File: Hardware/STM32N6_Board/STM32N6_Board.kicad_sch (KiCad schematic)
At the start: 0 parts

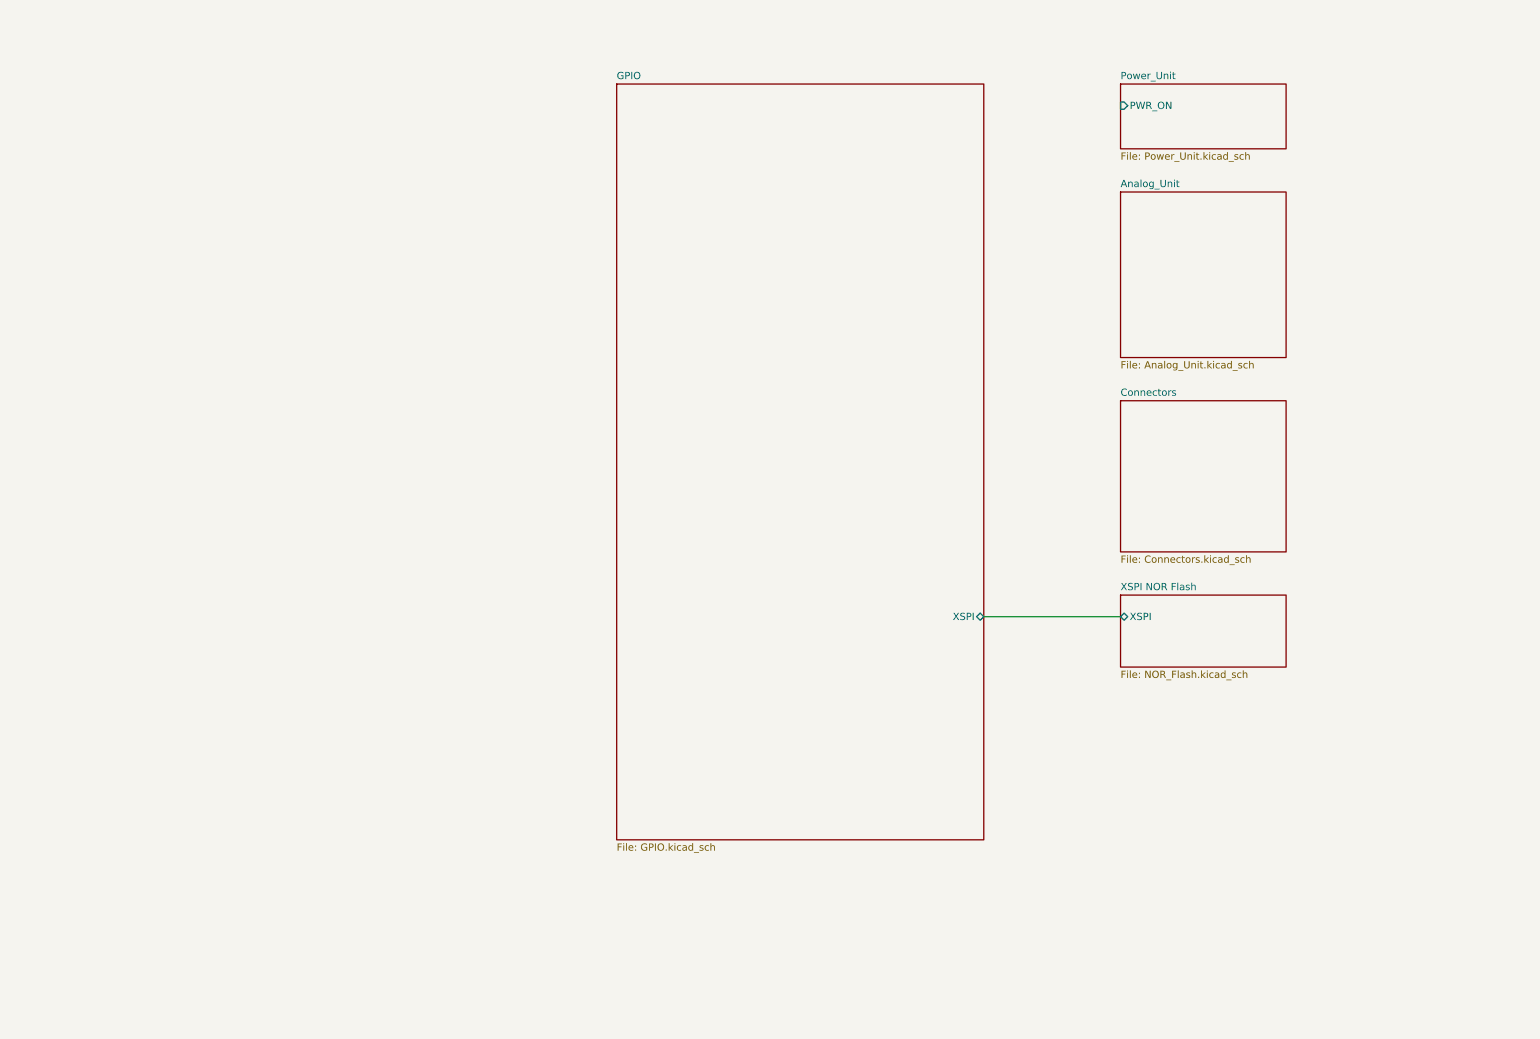
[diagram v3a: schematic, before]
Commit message: Completed wiring of the Analog unit.
- CSI and USB buses are created, yet to be connected with connectors
- Next will be pin selection, and drawing in FMC SDRAM
- Then will be routing GPIOs as buses, and connecting with connectors
- Finally, board layout.
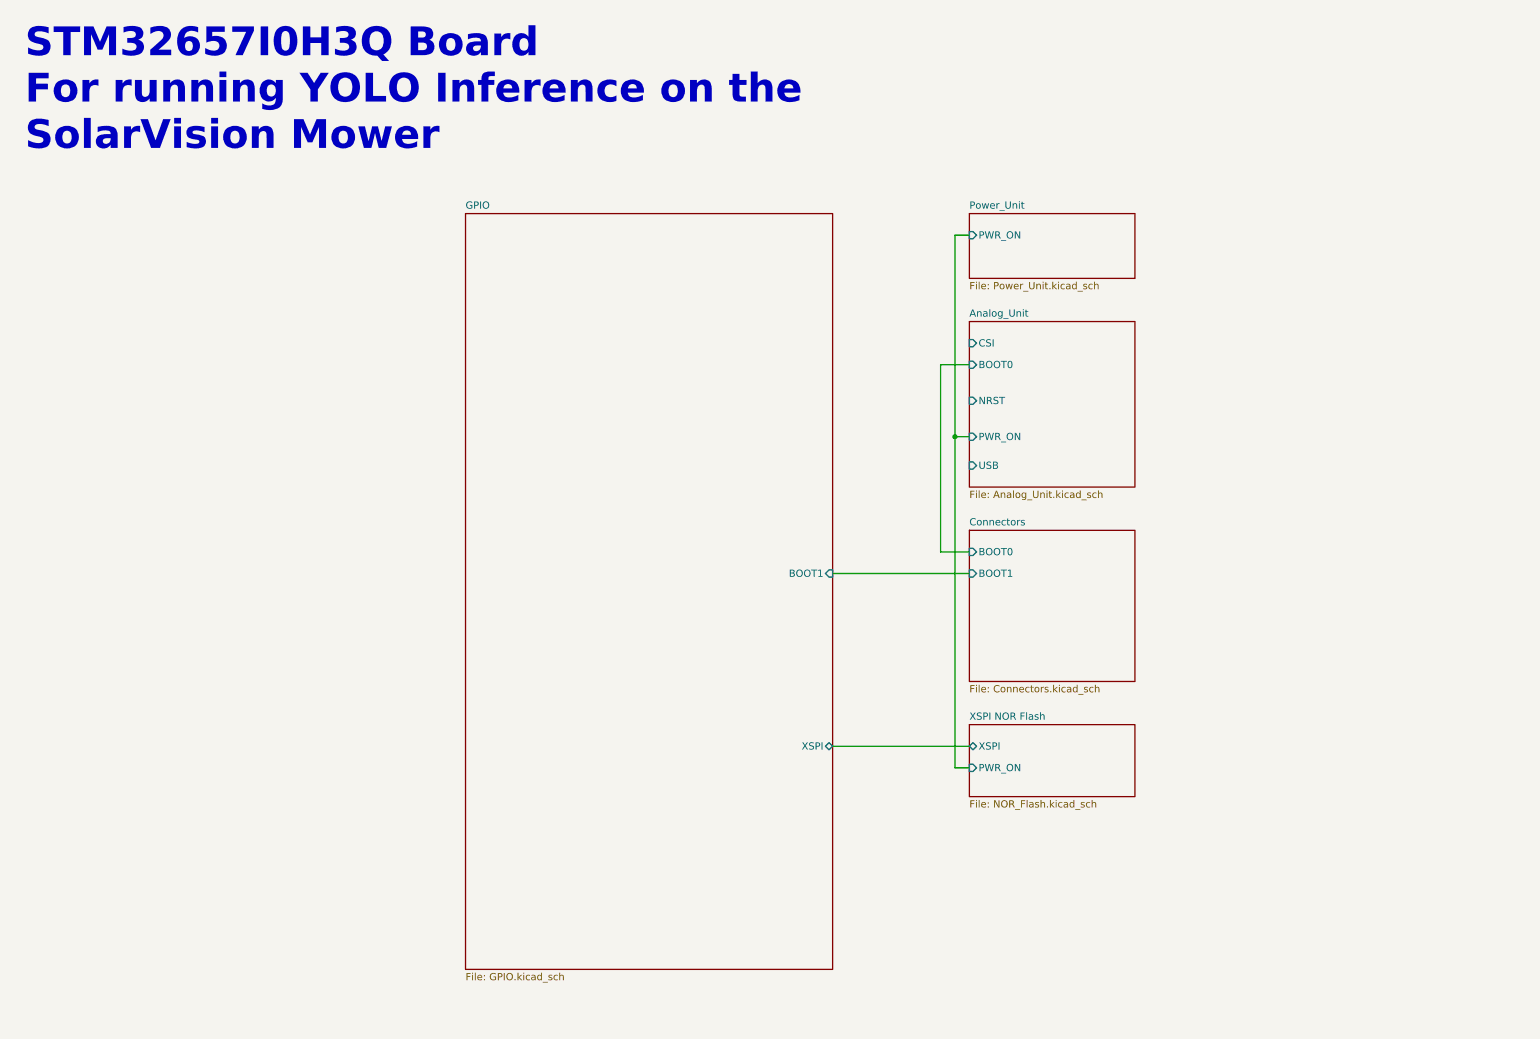
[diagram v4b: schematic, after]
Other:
- sheet Analog_Unit ports: added BOOT0, CSI, NRST, PWR_ON, USB; removed none
- sheet Connectors ports: added BOOT0, BOOT1; removed none
- sheet GPIO ports: added BOOT1; removed none
- sheet XSPI NOR Flash ports: added PWR_ON; removed none
- note added: "STM32657I0H3Q Board For running YOLO Inference on the SolarVision Mower"
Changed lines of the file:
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@@
 		(comment 1 "https://github.com/SolarVisionMower/SolarVision")
 	)
-	(wire
-		(pts
-			(xy 187.96 123.19) (xy 212.09 123.19)
+	(text "STM32657I0H3Q Board\nFor running YOLO Inference on the\nSolarVision Mower"
+		(exclude_from_sim no)
+		(at 18.796 19.05 0)
+		(effects
+			(font
+				(size 5.08 5.08)
+				(thickness 1.016)
+				(bold yes)
+			)
+			(justify left top)
+		)
+	)
+	(junction
+		(at 182.88 91.44)
+		(diameter 0)
+		(color 0 0 0 0)
+	)
+	(wire
+		(pts
+			(xy 182.88 55.88) (xy 182.88 91.44)
+		)
+		(stroke
+			(width 0)
+			(type default)
+		)
+	)
+	(wire
+		(pts
+			(xy 161.29 115.57) (xy 185.42 115.57)
+		)
+		(stroke
+			(width 0)
+			(type default)
+		)
+	)
+	(wire
+		(pts
+			(xy 182.88 149.86) (xy 182.88 91.44)
+		)
+		(stroke
+			(width 0)
+			(type default)
+		)
+	)
+	(wire
+		(pts
+			(xy 180.34 78.74) (xy 180.34 111.76)
+		)
+		(stroke
+			(width 0)
+			(type default)
+		)
+	)
+	(wire
+		(pts
+			(xy 161.29 146.05) (xy 185.42 146.05)
+		)
+		(stroke
+			(width 0)
+			(type default)
+		)
+	)
+	(wire
+		(pts
+			(xy 185.42 149.86) (xy 182.88 149.86)
+		)
+		(stroke
+			(width 0)
+			(type default)
+		)
+	)
+	(wire
+		(pts
+			(xy 185.42 55.88) (xy 182.88 55.88)
+		)
+		(stroke
+			(width 0)
+			(type default)
+		)
+	)
+	(wire
+		(pts
+			(xy 185.42 78.74) (xy 180.34 78.74)
+		)
+		(stroke
+			(width 0)
+			(type default)
+		)
+	)
+	(wire
+		(pts
+			(xy 182.88 91.44) (xy 185.42 91.44)
+		)
+		(stroke
+			(width 0)
+			(type default)
+		)
+	)
+	(wire
+		(pts
+			(xy 180.34 111.76) (xy 185.42 111.76)
 		)
 		(stroke
@@
 	)
 	(sheet
-		(at 123.19 29.21)
+		(at 96.52 52.07)
 		(size 64.77 133.35)
 		(exclude_from_sim no)
@@
 		)
 		(property "Sheetname" "GPIO"
-			(at 123.19 28.4984 0)
+			(at 96.52 51.3584 0)
 			(effects
 				(font
@@
 		)
 		(property "Sheetfile" "GPIO.kicad_sch"
-			(at 123.19 163.1446 0)
+			(at 96.52 186.0046 0)
 			(effects
 				(font
@@
 		)
 		(pin "XSPI" bidirectional
-			(at 187.96 123.19 0)
+			(at 161.29 146.05 0)
+			(effects
+				(font
+					(size 1.27 1.27)
+				)
+				(justify right)
+			)
+		)
+		(pin "BOOT1" input
+			(at 161.29 115.57 0)
 			(effects
 				(font
@@
 	)
 	(sheet
-		(at 212.09 119.38)
+		(at 185.42 142.24)
 		(size 29.21 12.7)
 		(exclude_from_sim no)
@@
 		)
 		(property "Sheetname" "XSPI NOR Flash"
-			(at 212.09 118.6684 0)
+			(at 185.42 141.5284 0)
 			(effects
 				(font
@@
 		)
 		(property "Sheetfile" "NOR_Flash.kicad_sch"
-			(at 212.09 132.6646 0)
+			(at 185.42 155.5246 0)
 			(effects
 				(font
@@
 		)
 		(pin "XSPI" bidirectional
-			(at 212.09 123.19 180)
+			(at 185.42 146.05 180)
+			(effects
+				(font
+					(size 1.27 1.27)
+				)
+				(justify left)
+			)
+		)
+		(pin "PWR_ON" input
+			(at 185.42 149.86 180)
 			(effects
 				(font
@@
 	)
 	(sheet
-		(at 212.09 48.26)
+		(at 185.42 71.12)
 		(size 29.21 29.21)
 		(exclude_from_sim no)
@@
 		)
 		(property "Sheetname" "Analog_Unit"
-			(at 212.09 47.5484 0)
+			(at 185.42 70.4084 0)
 			(effects
 				(font
@@
 		)
 		(property "Sheetfile" "Analog_Unit.kicad_sch"
-			(at 212.09 78.0546 0)
+			(at 185.42 100.9146 0)
 			(effects
 				(font
@@
 				)
 				(justify left top)
+			)
+		)
+		(pin "BOOT0" input
+			(at 185.42 78.74 180)
+			(effects
+				(font
+					(size 1.27 1.27)
+				)
+				(justify left)
+			)
+		)
+		(pin "NRST" input
+			(at 185.42 85.09 180)
+			(effects
+				(font
+					(size 1.27 1.27)
+				)
+				(justify left)
+			)
+		)
+		(pin "PWR_ON" input
+			(at 185.42 91.44 180)
+			(effects
+				(font
+					(size 1.27 1.27)
+				)
+				(justify left)
+			)
+		)
+		(pin "USB" input
+			(at 185.42 96.52 180)
+			(effects
+				(font
+					(size 1.27 1.27)
+				)
+				(justify left)
+			)
+		)
+		(pin "CSI" input
+			(at 185.42 74.93 180)
+			(effects
+				(font
+					(size 1.27 1.27)
+				)
+				(justify left)
 			)
 		)
@@
 	)
 	(sheet
-		(at 212.09 85.09)
+		(at 185.42 107.95)
 		(size 29.21 26.67)
 		(exclude_from_sim no)
@@
 		)
 		(property "Sheetname" "Connectors"
-			(at 212.09 84.3784 0)
+			(at 185.42 107.2384 0)
 			(effects
 				(font
@@
 		)
 		(property "Sheetfile" "Connectors.kicad_sch"
-			(at 212.09 112.3446 0)
+			(at 185.42 135.2046 0)
 			(effects
 				(font
@@
 				)
 				(justify left top)
+			)
+		)
+		(pin "BOOT0" input
+			(at 185.42 111.76 180)
+			(effects
+				(font
+					(size 1.27 1.27)
+				)
+				(justify left)
+			)
+		)
+		(pin "BOOT1" input
+			(at 185.42 115.57 180)
+			(effects
+				(font
+					(size 1.27 1.27)
+				)
+				(justify left)
 			)
 		)
@@
 	)
 	(sheet
-		(at 212.09 29.21)
+		(at 185.42 52.07)
 		(size 29.21 11.43)
 		(exclude_from_sim no)
@@
 		)
 		(property "Sheetname" "Power_Unit"
-			(at 212.09 28.4984 0)
+			(at 185.42 51.3584 0)
 			(effects
 				(font
@@
 		)
 		(property "Sheetfile" "Power_Unit.kicad_sch"
-			(at 212.09 41.2246 0)
+			(at 185.42 64.0846 0)
 			(effects
 				(font
@@
 		)
 		(pin "PWR_ON" input
-			(at 212.09 33.02 180)
-			(effects
-				(font
+			(at 185.42 55.88 180)
+			(effects
+				(font

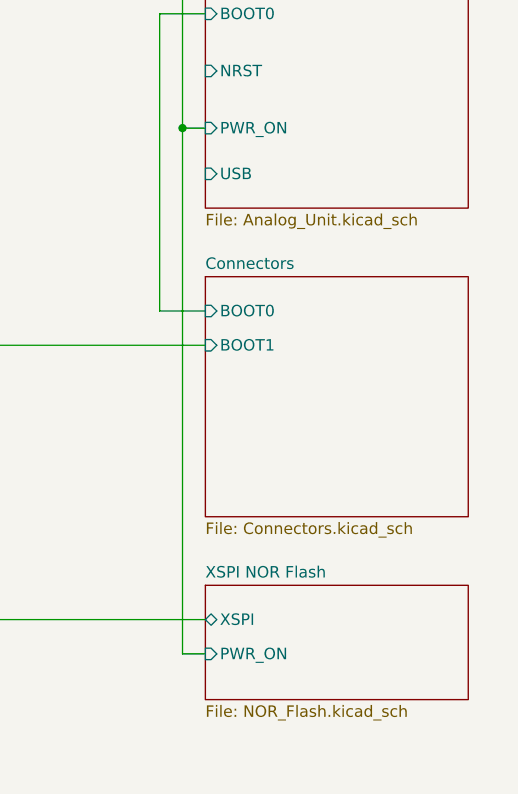
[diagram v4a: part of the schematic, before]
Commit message: Added and Updated some stuff
- Added layout guide for the IS42 SDRAM chip
- Modified reset pins wiring (now only on one reset button)
- Added design notes in docs/STM32N6/DesignNotes.md
- Updated PROGRESS.md
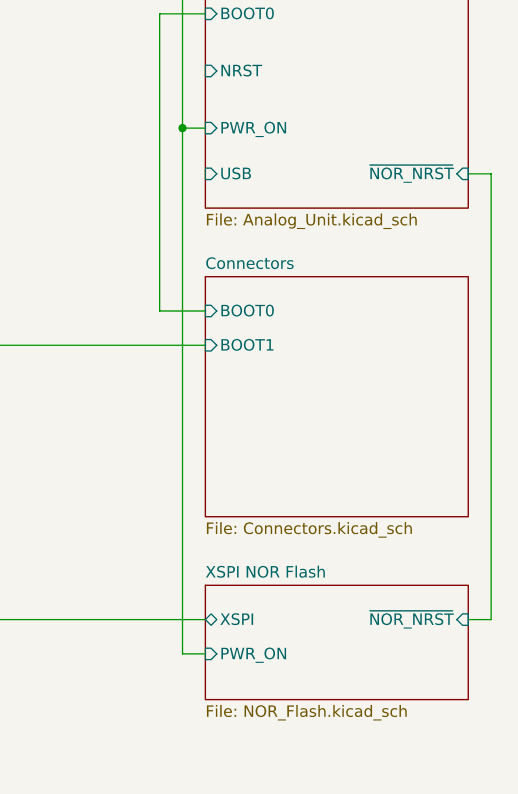
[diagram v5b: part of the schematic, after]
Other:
- sheet Analog_Unit ports: added ~{NOR_NRST}; removed none
- sheet XSPI NOR Flash ports: added ~{NOR_NRST}; removed none
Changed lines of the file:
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@@
+	(wire
+		(pts
+			(xy 217.17 146.05) (xy 214.63 146.05)
+		)
+		(stroke
+			(width 0)
+			(type default)
+		)
+	)
 	(wire
 		(pts
@@
 	(wire
 		(pts
+			(xy 214.63 96.52) (xy 217.17 96.52)
+		)
+		(stroke
+			(width 0)
+			(type default)
+		)
+	)
+	(wire
+		(pts
 			(xy 180.34 111.76) (xy 185.42 111.76)
+		)
+		(stroke
+			(width 0)
+			(type default)
+		)
+	)
+	(wire
+		(pts
+			(xy 217.17 96.52) (xy 217.17 146.05)
 		)
 		(stroke
@@
 			)
 		)
+		(pin "~{NOR_NRST}" input
+			(at 214.63 146.05 0)
+			(effects
+				(font
+					(size 1.27 1.27)
+				)
+				(justify right)
+			)
+		)
 		(instances
 			(project "STM32N6_Board"
@@
 			)
 		)
+		(pin "~{NOR_NRST}" input
+			(at 214.63 96.52 0)
+			(effects
+				(font
+					(size 1.27 1.27)
+				)
+				(justify right)
+			)
+		)
